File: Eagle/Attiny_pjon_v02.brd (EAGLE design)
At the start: 24.1 x 39.7 mm, 16 parts, among them IC2 78L05SMD

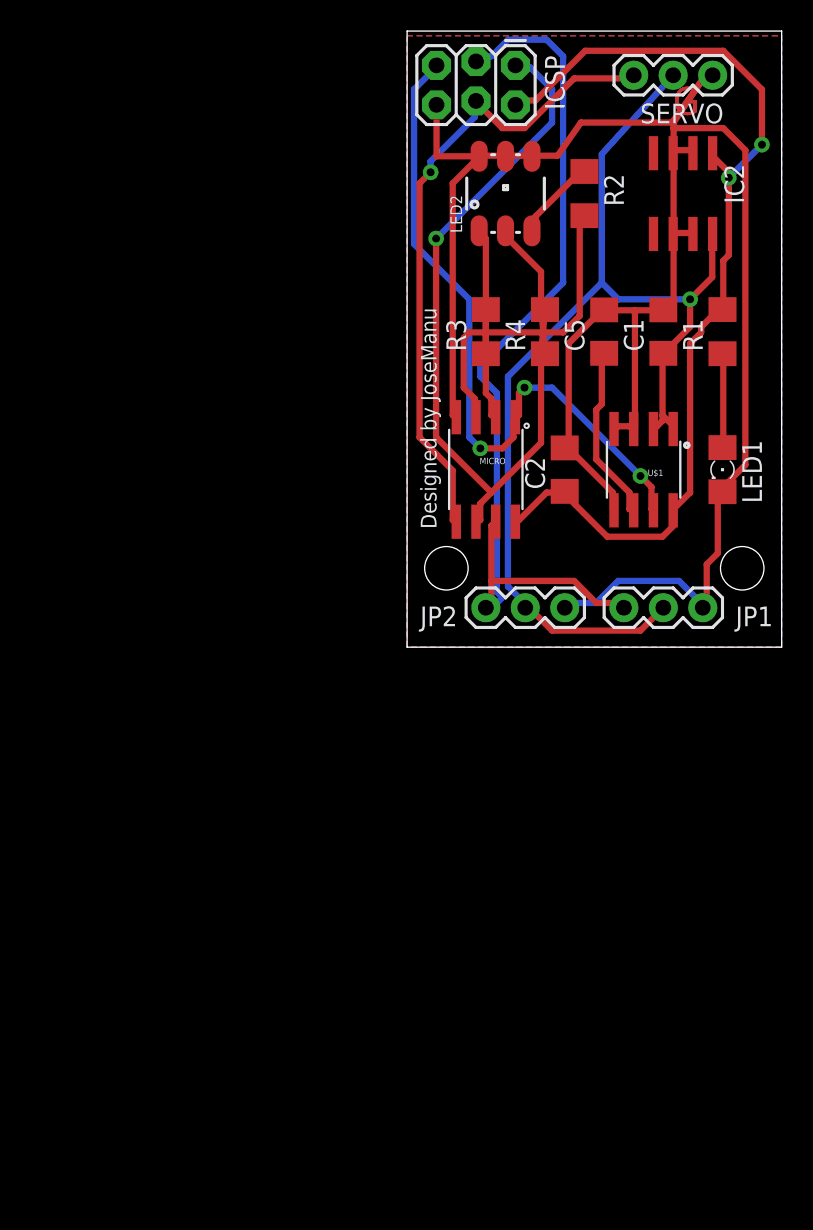
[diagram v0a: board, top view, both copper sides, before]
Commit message: Board V0.2
RGB LED Removed.
Added external oscillator, temperature sensor and a center hole
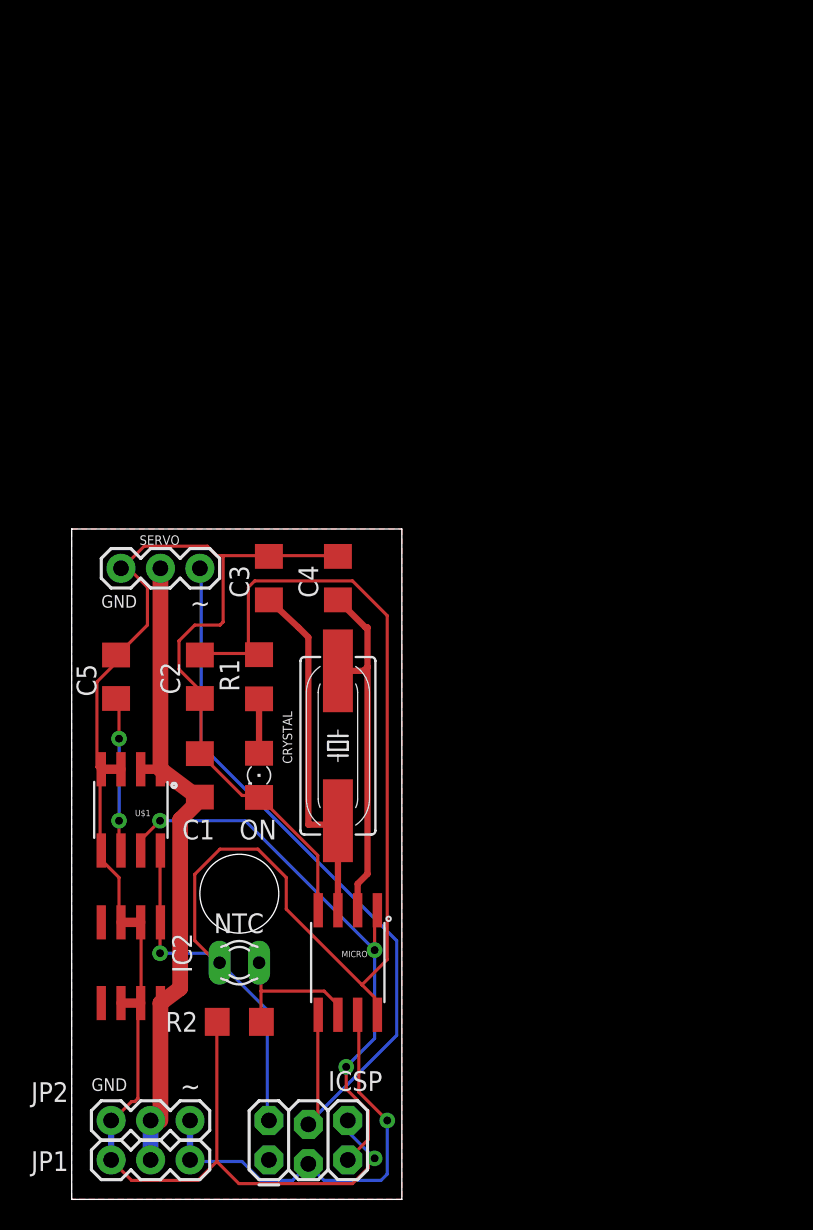
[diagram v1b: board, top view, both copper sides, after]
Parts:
- removed LED1: (no value), led:1206
- removed LED2: LED-TRICOLOR-5050NO_IC, SparkFun-LED:LED-TRICOLOR-5050
- removed R3, R4: 220, resistor:R1206
- added C3, C4: 22pF, rcl:C1206
- added CRYSTAL: (no value), SparkFun-FreqCtrl:HC49UP
- added NTC: 10K, ptc-ntc:P640
- added ON: (no value), led:1206
- R2: value 220 -> 10K
- moved ICSP 72.3 mm to (12.7, 2.54), turned to 0 degrees
- moved IC2 61.0 mm to (3.81, 15.2)
- moved R2 57.8 mm to (10.8, 11.4), turned to 0 degrees
- moved JP1 52.1 mm to (2.54, 2.54), turned to 0 degrees
- moved SERVO 49.6 mm to (3.17, 40.6), turned to 0 degrees
- moved JP2 44.1 mm to (2.54, 5.08), turned to 0 degrees
- moved C1 41.3 mm to (8.26, 27.3)
- moved U$1 39.6 mm to (3.81, 25.1)
- moved C5 38.5 mm to (2.86, 33.7)
- moved R1 37.2 mm to (12.1, 33.7)
- moved MICRO 33.0 mm to (17.8, 15.2)
- moved C2 27.0 mm to (8.26, 33.7), turned to 270 degrees
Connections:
- removed net N$1: MICRO.3, R2.2
- removed net N$3: MICRO.2, R3.2
- removed net N$4: LED2.3, R2.1
- removed net N$5: LED2.1, R3.1
- removed net N$7: LED2.2, R4.1
- new net NTC: MICRO.6, NTC.1, R2.2
- new net XTAL: C4.1, CRYSTAL.2, MICRO.2
- new net XTAL2: C3.1, CRYSTAL.1, MICRO.3
- net GND: now also C3.2, C4.2, ON.C, R2.1; no longer LED1.C, LED2.4, LED2.5, LED2.6
- net MISO: no longer MICRO.6, R4.2
- net N$8: now also ON.A; no longer LED1.A
- net VO: now also NTC.2
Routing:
- net MISO: track 49.0 -> 0.00 mm, vias 1 -> 0
- net PJON: track 61.1 -> 27.9 mm, vias 0 -> 1
- net VCC: track 70.6 -> 42.8 mm, vias 1 -> 0
- net VO: track 63.5 -> 90.7 mm, vias 2 -> 1
- net XTAL2: track 0.00 -> 23.7 mm
- net XTAL: track 0.00 -> 23.1 mm
- net N$1: track 20.2 -> 0.00 mm
- net GND: track 135.1 -> 121.9 mm, vias 0 -> 1
- net NTC: track 0.00 -> 9.89 mm
- net N$7: track 9.06 -> 0.00 mm
- net MOSI: track 41.9 -> 50.8 mm, vias 1 -> 0
- net N$5: track 8.08 -> 0.00 mm
- net ADC0: track 45.4 -> 37.8 mm
- net N$3: track 7.26 -> 0.00 mm
- net N$4: track 5.36 -> 0.00 mm
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- removed copper zone on layer 16, net GND
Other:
- board size 24.1 x 39.7 mm -> 21.3 x 43.2 mm
- board text added: "Advanced Servo Controller V0.2 Designed By Ardumania Thanks to @gioblu and @JavierIH"
- board text added: "GND"
- board text added: "~"
- board text removed: "Designed by JoseManu"
- board text removed: "G"
- board text removed: "S"
- board text removed: "Vcc"
